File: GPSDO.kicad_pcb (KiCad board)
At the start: 2 copper layers, 74 parts, among them J1 Conn_Coaxial, J2 GPS_CONN, J3 Conn_Coaxial, J4 Conn_Coaxial, J5 Conn_Coaxial, J6 Conn_Coaxial, J7 LCD_CONN, J8 Barrel_Jack, J9 TOUCH_CONN, SW1 RESET_BTN, U1 REF3450, U11 74AUC1G74, U14 MC3487DX, U16 L7805, U2 74AUC1G125, U3 AD5680, U4 NB3N551MN, U5 LTC2050IS8, U6 AVR32DB28x-xSO, U7 74AUC1G125, U8 74HC390, X1 OCXO-14

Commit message: Updated schematic
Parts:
- added C11: 100u 35V, Capacitor_SMD:C_Elec_6.3x7.7, F.Cu at (110.1, 126.3)
- added C19: 100u 35V, Capacitor_SMD:CP_Elec_8x10, F.Cu at (87.6, 127.1)
- added C20: 100u 35V, Capacitor_SMD:CP_Elec_8x10, F.Cu at (87.6, 137.0)
- added C28: 100n, Capacitor_SMD:C_0805_2012Metric_Pad1.18x1.45mm_HandSolder, F.Cu at (94.4, 150.7)
- added C29: 100n 10V MLCC, Capacitor_SMD:C_0805_2012Metric_Pad1.18x1.45mm_HandSolder, F.Cu at (94.4, 147.7)
- added C30: 100n 10V MLCC, Capacitor_SMD:C_0805_2012Metric_Pad1.18x1.45mm_HandSolder, F.Cu at (105.7, 137.8)
- added C36: 100n 10V MLCC, Capacitor_SMD:C_0805_2012Metric_Pad1.18x1.45mm_HandSolder, F.Cu at (100.5, 141.7)
- added C37: 100n 10V MLCC, Capacitor_SMD:C_0805_2012Metric_Pad1.18x1.45mm_HandSolder, F.Cu at (105.7, 140.8)
- added C38: 100n 10V MLCC, Capacitor_SMD:C_0805_2012Metric_Pad1.18x1.45mm_HandSolder, F.Cu at (111.7, 131.9)
- added C39: 100n 10V MLCC, Capacitor_SMD:C_0805_2012Metric_Pad1.18x1.45mm_HandSolder, F.Cu at (100.5, 144.7)
- added C40: 100n 10V MLCC, Capacitor_SMD:C_0805_2012Metric_Pad1.18x1.45mm_HandSolder, F.Cu at (111.7, 134.9)
- added C41: 100n 10V MLCC, Capacitor_SMD:C_0805_2012Metric_Pad1.18x1.45mm_HandSolder, F.Cu at (117.5, 126.7)
- added R11: 0R, Resistor_SMD:R_0805_2012Metric_Pad1.20x1.40mm_HandSolder, F.Cu at (117.5, 129.7)
- added U10: MC7805BDTRKG, Package_TO_SOT_SMD:TO-252-2, F.Cu at (76.0, 148.3)
- added U9: L7805CV, Package_TO_SOT_THT:TO-220-3_Horizontal_TabDown, F.Cu at (73.2, 142.5)
- C1: value 10u -> 100u 35V; footprint Capacitor_THT:CP_Radial_D5.0mm_P2.00mm -> Capacitor_SMD:C_Elec_6.3x7.7
- C10: value 1u -> 100u 35V; footprint Capacitor_THT:CP_Radial_D5.0mm_P2.00mm -> Capacitor_SMD:C_Elec_6.3x7.7
- C17: value 10u -> 100n low ESR; footprint Capacitor_THT:CP_Radial_D5.0mm_P2.00mm -> Capacitor_SMD:C_0805_2012Metric_Pad1.18x1.45mm_HandSolder
- C18, C9: value 10u -> 10u 25V; footprint Capacitor_THT:CP_Radial_D5.0mm_P2.00mm -> Capacitor_SMD:C_1210_3225Metric_Pad1.33x2.70mm_HandSolder
- C22: value 10u -> 100u 35V; footprint Capacitor_SMD:C_Elec_4x5.4 -> Capacitor_SMD:C_Elec_6.3x7.7
- C32, C33, C34: value 100u -> 100u 35V; footprint Capacitor_THT:CP_Radial_D5.0mm_P2.00mm -> Capacitor_SMD:CP_Elec_8x10
- C5: value 10u -> 100u 35V; footprint Capacitor_THT:CP_Radial_D5.0mm_P2.00mm -> Capacitor_SMD:CP_Elec_8x10
- C7: value tot=15pF? -> total OCXO load=15pF?
- moved C18 61.8 mm to (106.3, 134.2)
- moved C1 59.5 mm to (98.3, 136.1)
- moved C9 59.1 mm to (95.0, 144.0)
- moved C17 58.6 mm to (117.5, 123.7)
- moved C10 44.1 mm to (87.1, 146.0)
- moved C5 42.6 mm to (99.4, 127.1)
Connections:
- C17 pad 1: Net-(C17-Pad1) -> Net-(R3-Pad2)
- C18 pad 1: +5VA -> Net-(R3-Pad2)
- C32 pad 1: Net-(C32-Pad1) -> /7VIN
- C32 pad 2: GND -> GNDA
- C33 pad 1: +5VD -> +5VA
- C33 pad 2: GND -> GNDA
- C34 pad 1: +5VD -> +5VA
- C34 pad 2: GND -> GNDA
- C35 pad 1: GND -> GNDA
- C35 pad 2: +5VD -> +5VA
- C5 pad 1: Net-(C3-Pad1) -> +5VA
- C9 pad 1: +5VA -> Net-(C3-Pad1)
- J3 pad 1: Net-(C36-Pad1) -> Net-(J3-Pad1)
- J3 pad 2: Net-(C37-Pad1) -> Net-(J3-Pad2)
- J4 pad 1: Net-(C38-Pad1) -> Net-(J4-Pad1)
- J4 pad 2: Net-(C39-Pad1) -> Net-(J4-Pad2)
- J5 pad 1: Net-(C40-Pad1) -> Net-(J5-Pad1)
- J5 pad 2: Net-(C41-Pad1) -> Net-(J5-Pad2)
- J6 pad 1: Net-(C42-Pad1) -> Net-(J6-Pad1)
- J6 pad 2: Net-(C43-Pad1) -> Net-(J6-Pad2)
- J8 pad 1: Net-(C32-Pad1) -> /7VIN
- J8 pad 2: GND -> GNDA
- R3 pad 2: Net-(C17-Pad1) -> Net-(R3-Pad2)
- U14 pad 10: Net-(C41-Pad2) -> Net-(U14-Pad10)
- U14 pad 11: Net-(C40-Pad2) -> Net-(U14-Pad11)
- U14 pad 13: Net-(C42-Pad2) -> Net-(U14-Pad13)
- U14 pad 14: Net-(C43-Pad2) -> Net-(U14-Pad14)
- U14 pad 2: Net-(C37-Pad2) -> Net-(U14-Pad2)
- U14 pad 3: Net-(C36-Pad2) -> Net-(U14-Pad3)
- U14 pad 5: Net-(C38-Pad2) -> Net-(U14-Pad5)
- U14 pad 6: Net-(C39-Pad2) -> Net-(U14-Pad6)
- U5 pad 3: Net-(C17-Pad1) -> Net-(R3-Pad2)

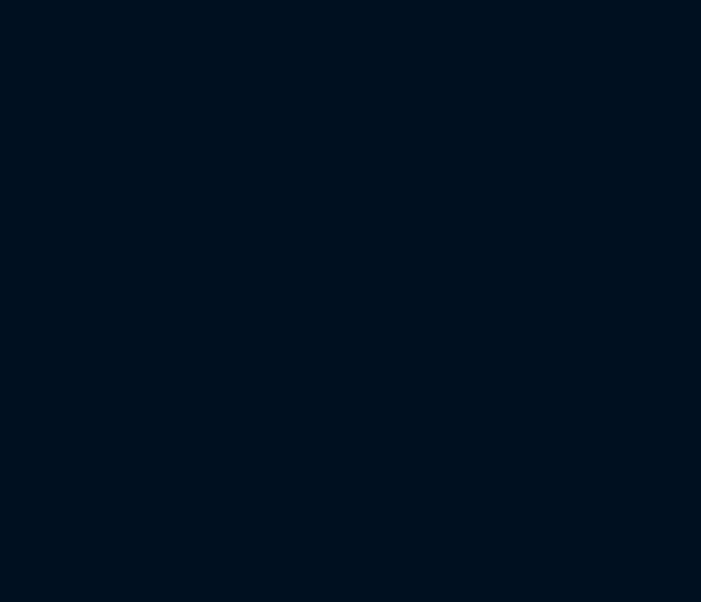
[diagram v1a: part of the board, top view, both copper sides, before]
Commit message: Added pulse delay in TIC
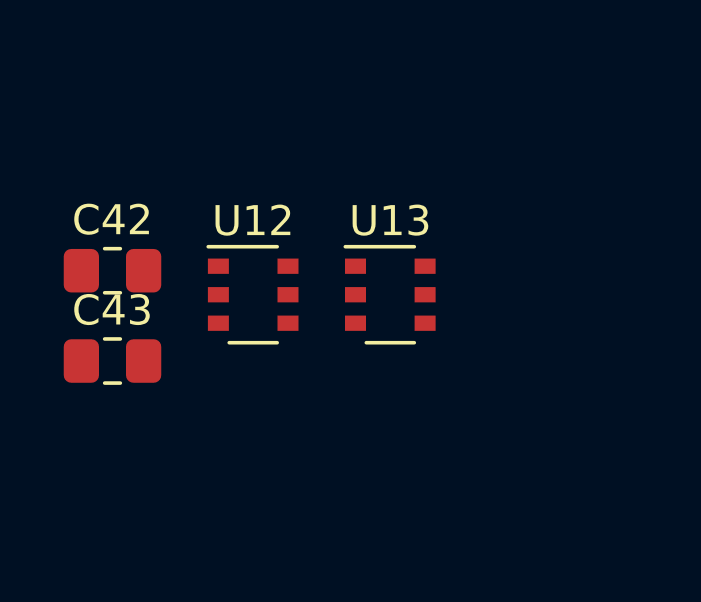
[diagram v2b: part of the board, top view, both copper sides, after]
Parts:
- added C42: 100n, Capacitor_SMD:C_0805_2012Metric_Pad1.18x1.45mm_HandSolder, F.Cu at (0.51, 20.7)
- added C43: 100n, Capacitor_SMD:C_0805_2012Metric_Pad1.18x1.45mm_HandSolder, F.Cu at (0.51, 23.7)
- added U12: 74AUC2G04, Package_SO:TSOP-6_1.65x3.05mm_P0.95mm, F.Cu at (5.20, 21.5)
- added U13: 74AUC2G04, Package_SO:TSOP-6_1.65x3.05mm_P0.95mm, F.Cu at (9.77, 21.5)
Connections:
- J1 pad 1: /PPS_SIG -> /PPS_SIG_3V3
- U11 pad 1: /MAIN_CLK_4 -> /uC_CLK
- U6 pad 22: /MAIN_CLK_4 -> /uC_CLK

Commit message: selected TIC components
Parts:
- removed R5, R7: 2k2, Resistor_SMD:R_0805_2012Metric_Pad1.20x1.40mm_HandSolder
- removed U16: L7805, Package_TO_SOT_THT:TO-220-3_Vertical
- moved H4 186.9 mm to (239.4, 125.0)
- moved H2 150.3 mm to (239.4, 23.5)
- moved H1 110.2 mm to (118.1, 140.0)
- moved J8 100.7 mm to (24.6, 128.9)
- moved C35 82.6 mm to (37.3, 104.9), turned to 180 degrees
- moved H3 61.7 mm to (114.4, 29.1)
- moved U9 55.0 mm to (22.2, 121.8)
- moved SW1 38.5 mm to (62.0, 73.0)
- moved C36 34.5 mm to (209.3, 95.4)
- moved C37 34.5 mm to (209.4, 99.3)
- moved C38 34.5 mm to (209.0, 80.4)
- moved C39 34.5 mm to (208.9, 76.8)
- moved C41 34.5 mm to (209.0, 63.5)
- moved C42 34.5 mm to (208.5, 47.1)
- moved C43 34.5 mm to (208.6, 43.2)
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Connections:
- J2 pad 1: unconnected-(J2-Pad1) -> +5VD
- J2 pad 2: unconnected-(J2-Pad2) -> /GPS_TXD
- J2 pad 3: unconnected-(J2-Pad3) -> /GPS_RXD
- J2 pad 4: unconnected-(J2-Pad4) -> GND

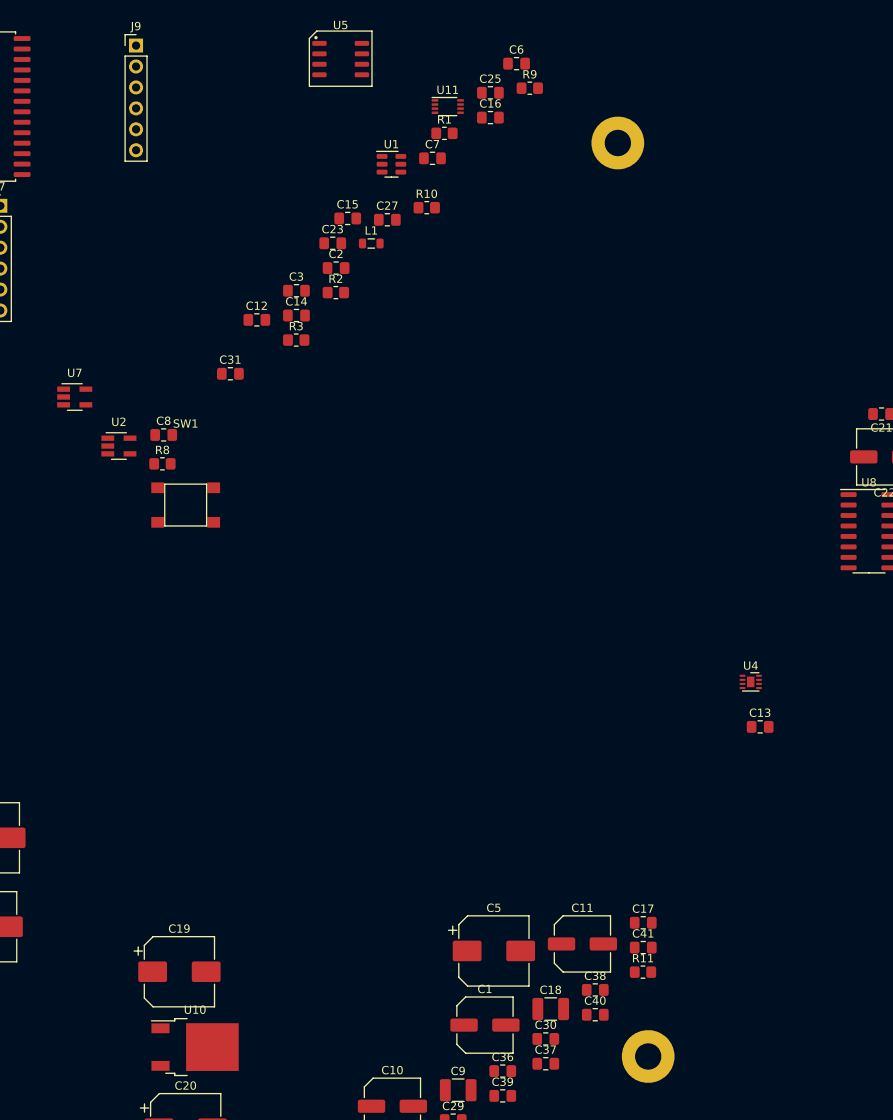
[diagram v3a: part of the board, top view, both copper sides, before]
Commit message: Added LEDs, modified SPI
All SPI uses the same interface now.
Added extra clocksource to a gpio pin, I don't know whether the internal systick timer will be configurable enough to count ticks
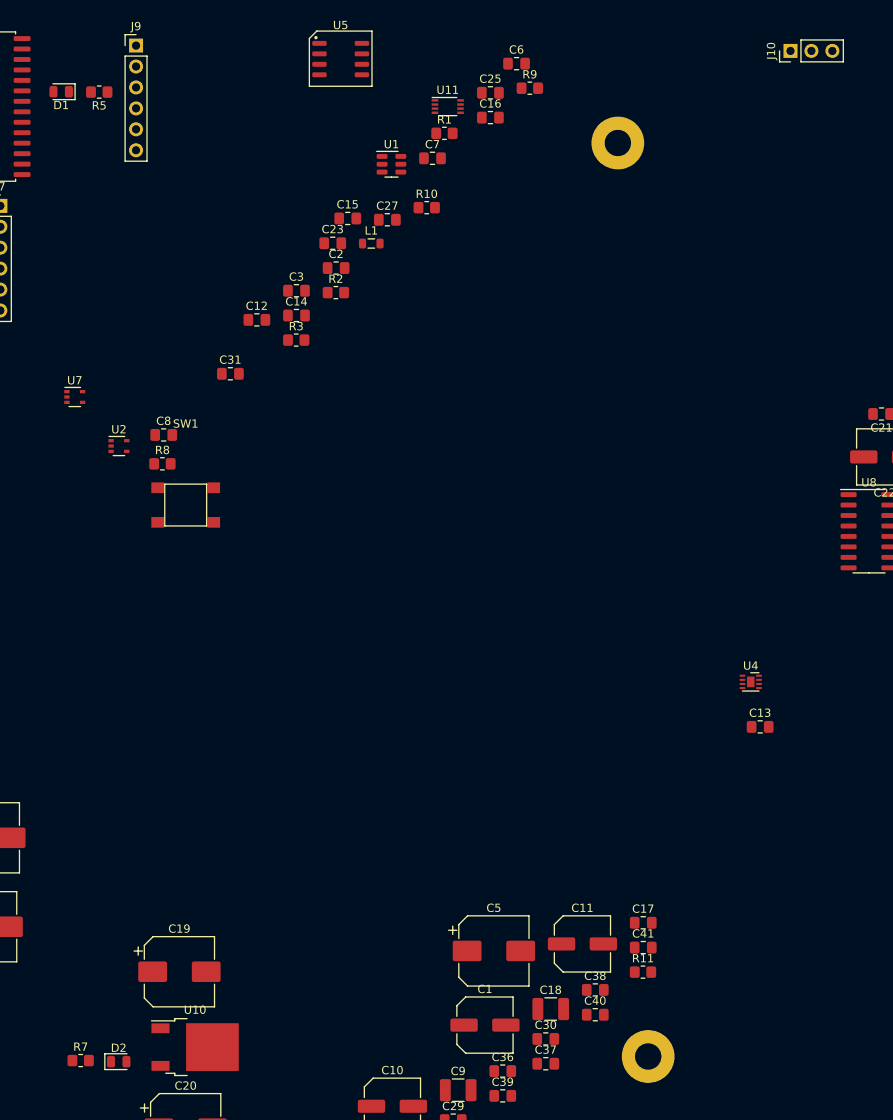
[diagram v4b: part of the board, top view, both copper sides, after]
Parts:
- added D1: LED, LED_SMD:LED_0805_2012Metric, F.Cu at (46.9, 22.9)
- added D2: LED, LED_SMD:LED_0805_2012Metric, F.Cu at (53.8, 140.6)
- added J10: PROG, Connector_PinHeader_2.54mm:PinHeader_1x03_P2.54mm_Vertical, F.Cu at (135.4, 17.9)
- added R5: 270R, Resistor_SMD:R_0805_2012Metric_Pad1.20x1.40mm_HandSolder, F.Cu at (51.5, 22.9)
- added R7: 270R, Resistor_SMD:R_0805_2012Metric_Pad1.20x1.40mm_HandSolder, F.Cu at (49.2, 140.4)
- C31: value 470p -> 680p
- R9: value 200R -> 150
- U2, U7: value 74AUC1G125 -> 74LVC1G125SE-7; footprint Package_TO_SOT_SMD:SOT-23-5_HandSoldering -> Package_TO_SOT_SMD:SOT-353_SC-70-5
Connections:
- C36 pad 1: Net-(U14-Pad5) -> Net-(C36-Pad1)
- C36 pad 2: Net-(J4-Pad1) -> Net-(C36-Pad2)
- C37 pad 1: Net-(U14-Pad6) -> Net-(C37-Pad1)
- C37 pad 2: Net-(J4-Pad2) -> Net-(C37-Pad2)
- C38 pad 1: Net-(U14-Pad11) -> Net-(C38-Pad1)
- C38 pad 2: Net-(J5-Pad1) -> Net-(C38-Pad2)
- C39 pad 1: Net-(U14-Pad10) -> Net-(C39-Pad1)
- C39 pad 2: Net-(J5-Pad2) -> Net-(C39-Pad2)
- C40 pad 1: Net-(U14-Pad13) -> Net-(C40-Pad1)
- C40 pad 2: Net-(J6-Pad1) -> Net-(C40-Pad2)
- C41 pad 1: Net-(U14-Pad14) -> Net-(C41-Pad1)
- C41 pad 2: Net-(J6-Pad2) -> Net-(C41-Pad2)
- J4 pad 1: Net-(J4-Pad1) -> Net-(C36-Pad2)
- J4 pad 2: Net-(J4-Pad2) -> Net-(C37-Pad2)
- J5 pad 1: Net-(J5-Pad1) -> Net-(C38-Pad2)
- J5 pad 2: Net-(J5-Pad2) -> Net-(C39-Pad2)
- J6 pad 1: Net-(J6-Pad1) -> Net-(C40-Pad2)
- J6 pad 2: Net-(J6-Pad2) -> Net-(C41-Pad2)
- U12 pad 1: /MAIN_CLK_4 -> /MAIN_CLK_3
- U14 pad 10: Net-(U14-Pad10) -> Net-(C39-Pad1)
- U14 pad 11: Net-(U14-Pad11) -> Net-(C38-Pad1)
- U14 pad 13: Net-(U14-Pad13) -> Net-(C40-Pad1)
- U14 pad 14: Net-(U14-Pad14) -> Net-(C41-Pad1)
- U14 pad 5: Net-(U14-Pad5) -> Net-(C36-Pad1)
- U14 pad 6: Net-(U14-Pad6) -> Net-(C37-Pad1)
- U6 pad 2: /LCD_MOSI -> /~{LCD_SS}
- U6 pad 23: /FF_RESET -> Net-(U6-Pad23)
- U6 pad 24: /FF_SET -> /MAIN_CLK_4
- U6 pad 3: /LCD_MISO -> /FF_RESET
- U6 pad 4: /LCD_SCK -> /FF_SET
- U6 pad 5: /~{LCD_SS} -> /TOUCH_IRQ

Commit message: some pcb placing
finding optimal location on the pcb
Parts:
- removed the C36 at (209.3, 95.4)
- removed the C37 at (209.4, 99.3)
- removed the C38 at (209.0, 80.4)
- removed the C39 at (208.9, 76.8)
- removed the C40 at (209.0, 58.8)
- removed the C41 at (209.0, 63.5)
- removed the C42 at (208.5, 47.1)
- removed the C43 at (208.6, 43.2)
- C7: value total OCXO load=15pF? -> 10pF
- moved U1 288.4 mm to (78.4, 319.9)
- moved C6 286.2 mm to (76.5, 304.5), turned to 90 degrees
- moved U5 276.3 mm to (89.3, 295.0), turned to 90 degrees
- moved C2 275.7 mm to (74.3, 319.9), turned to 90 degrees
- moved C3 267.3 mm to (78.4, 314.3), turned to 180 degrees
- moved C16 263.4 mm to (87.2, 289.2), turned to 180 degrees
- moved R3 253.2 mm to (86.6, 305.9)
- moved U3 251.4 mm to (80.4, 304.5), turned to 90 degrees
- moved L1 244.5 mm to (75.1, 285.6), turned to 90 degrees
- moved X1 243.4 mm to (89.7, 284.6), turned to 90 degrees
- moved U12 242.9 mm to (78.0, 253.2), turned to 180 degrees
- moved C42 242.8 mm to (92.2, 245.5), turned to -90 degrees
- moved C43 242.1 mm to (74.5, 254.3), turned to 90 degrees
- moved U6 240.4 mm to (36.2, 265.0)
- moved R5 240.2 mm to (49.9, 263.1)
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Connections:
- R8 pad 2: +5V -> +5VD

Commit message: LCD conn
Updated LCD & touch connector
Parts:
- removed D1: LED, LED_SMD:LED_0805_2012Metric
- removed J9: TOUCH_CONN, Connector_PinHeader_2.54mm:PinHeader_1x06_P2.54mm_Vertical
- removed R5: 270R, Resistor_SMD:R_0805_2012Metric_Pad1.20x1.40mm_HandSolder
- added C44: 100n, Capacitor_SMD:C_0805_2012Metric_Pad1.18x1.45mm_HandSolder, F.Cu at (57.3, 238.5)
- added C45: 100u 35V, Capacitor_SMD:C_Elec_6.3x7.7, F.Cu at (56.8, 233.4)
- J7: value LCD_CONN -> DISP_MODULE; footprint Connector_PinHeader_2.54mm:PinHeader_1x06_P2.54mm_Vertical -> Connector_PinHeader_2.54mm:PinHeader_1x14_P2.54mm_Vertical
- moved J10 289.6 mm to (23.5, 285.0), turned to -90 degrees
- moved R1 245.8 mm to (52.2, 270.3), turned to 180 degrees
- moved C15 239.7 mm to (15.4, 268.6)
- moved R10 232.5 mm to (95.8, 269.4)
- moved J2 228.8 mm to (41.5, 285.0), turned to -90 degrees
- moved C12 222.4 mm to (12.0, 265.1)
- moved C14 222.4 mm to (16.8, 264.5)
- moved C25 220.8 mm to (102.9, 243.7)
- moved C23 214.8 mm to (101.9, 254.9)
- moved C27 211.8 mm to (101.7, 249.7)
- moved C8 206.4 mm to (47.1, 270.5)
- moved J7 205.6 mm to (20.3, 241.4), turned to 90 degrees
- moved SW1 202.6 mm to (49.8, 275.2)
- moved C1 182.3 mm to (109.9, 249.8)
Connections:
- J7 pad 1: unconnected-(J7-Pad1) -> /TOUCH_IRQ
- J7 pad 2: unconnected-(J7-Pad2) -> /LCD_MISO
- J7 pad 3: unconnected-(J7-Pad3) -> /DAC_MOSI
- J7 pad 4: unconnected-(J7-Pad4) -> /~{TOUCH_SS}
- J7 pad 5: unconnected-(J7-Pad5) -> /DAC_SCK
- J7 pad 6: unconnected-(J7-Pad6) -> /LCD_MISO
- U6 pad 23: Net-(U6-Pad23) -> /LCD_DCRS
- U6 pad 24: /MAIN_CLK_4 -> /LCD_RESET
- U6 pad 27: /DAC_MISO -> /LCD_MISO

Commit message: Updated output stage and a few bugs
Different driver, some layout moving
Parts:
- C29, C30, C36, C37, C38, C39, C40, C41: value 100n 10V MLCC -> 22nF 630V
- U14: value MC3487DX -> DS34C87T
- moved J2 259.5 mm to (170.3, 59.7)
- moved J10 255.6 mm to (156.6, 66.8), turned to 0 degrees
- moved C15 236.7 mm to (165.7, 85.9), turned to -90 degrees
- moved SW1 236.4 mm to (165.1, 68.8), turned to 90 degrees
- moved C14 234.6 mm to (155.3, 75.2)
- moved R1 230.7 mm to (160.1, 66.4), turned to -90 degrees
- moved C8 229.0 mm to (160.4, 71.5), turned to 90 degrees
- moved C12 222.6 mm to (151.5, 91.7), turned to 90 degrees
- moved U6 217.8 mm to (154.9, 82.4), turned to 90 degrees
- moved U1 201.6 mm to (134.4, 126.2)
- moved C2 201.6 mm to (130.3, 126.2)
- moved C3 201.6 mm to (134.4, 120.6)
- moved C9 201.6 mm to (134.5, 116.1)
- moved C6 201.2 mm to (140.2, 113.7), turned to 0 degrees
- moved C11 196.6 mm to (135.9, 108.5), turned to 90 degrees
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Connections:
- net /20Mc_CLK renamed /MAIN_CLK_2
- U12 pad 1: /MAIN_CLK_3 -> /MAIN_CLK_4
- U3 pad 6: /DAC_SLK -> /DAC_SCK
- U8 pad 15: /MAIN_CLK_1 -> /MAIN_CLK_3
- U8 pad 4: /MAIN_CLK_1 -> /MAIN_CLK_3
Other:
- board text added: "TODO: align conn to housing"
